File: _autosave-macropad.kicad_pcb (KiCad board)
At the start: 2 copper layers, 34 parts, among them SW1 RotaryEncoder_Switch, U1 MOUDLE-SEEEDUINO-XIAO

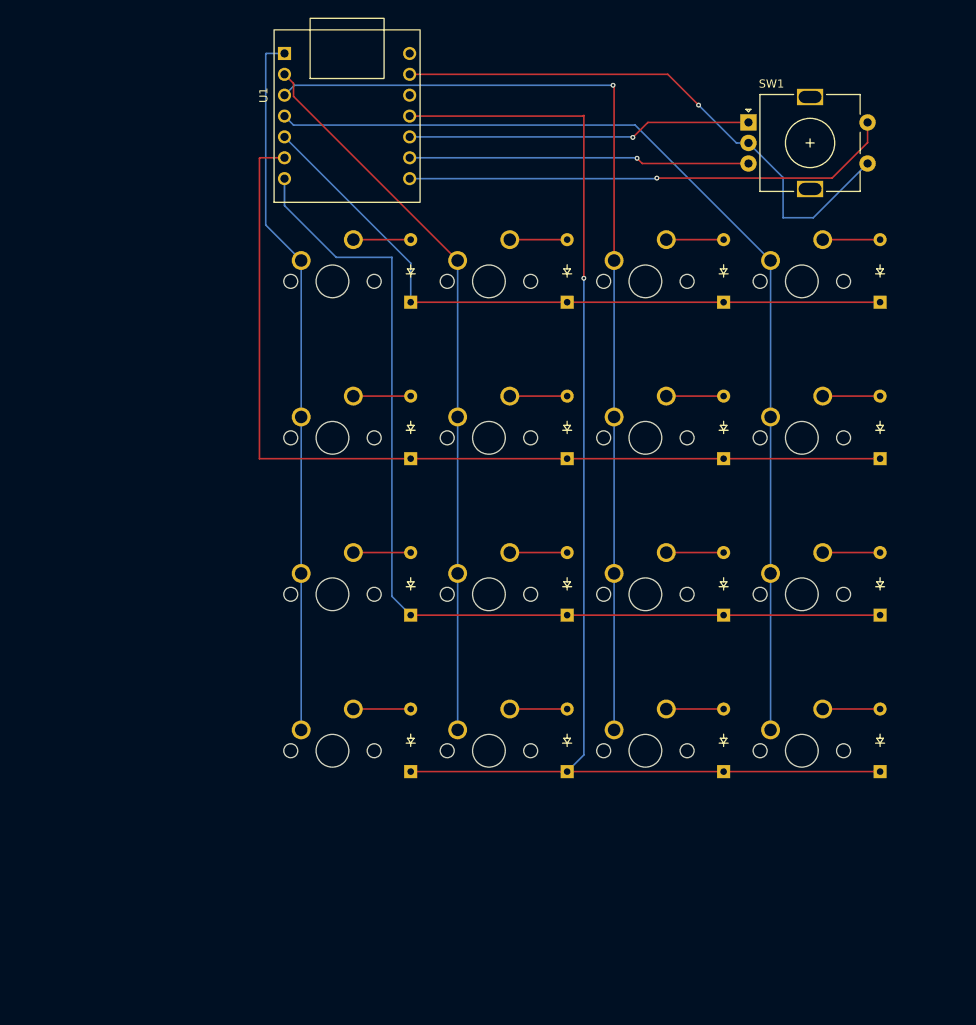
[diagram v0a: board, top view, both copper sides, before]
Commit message: Make cutout and holes
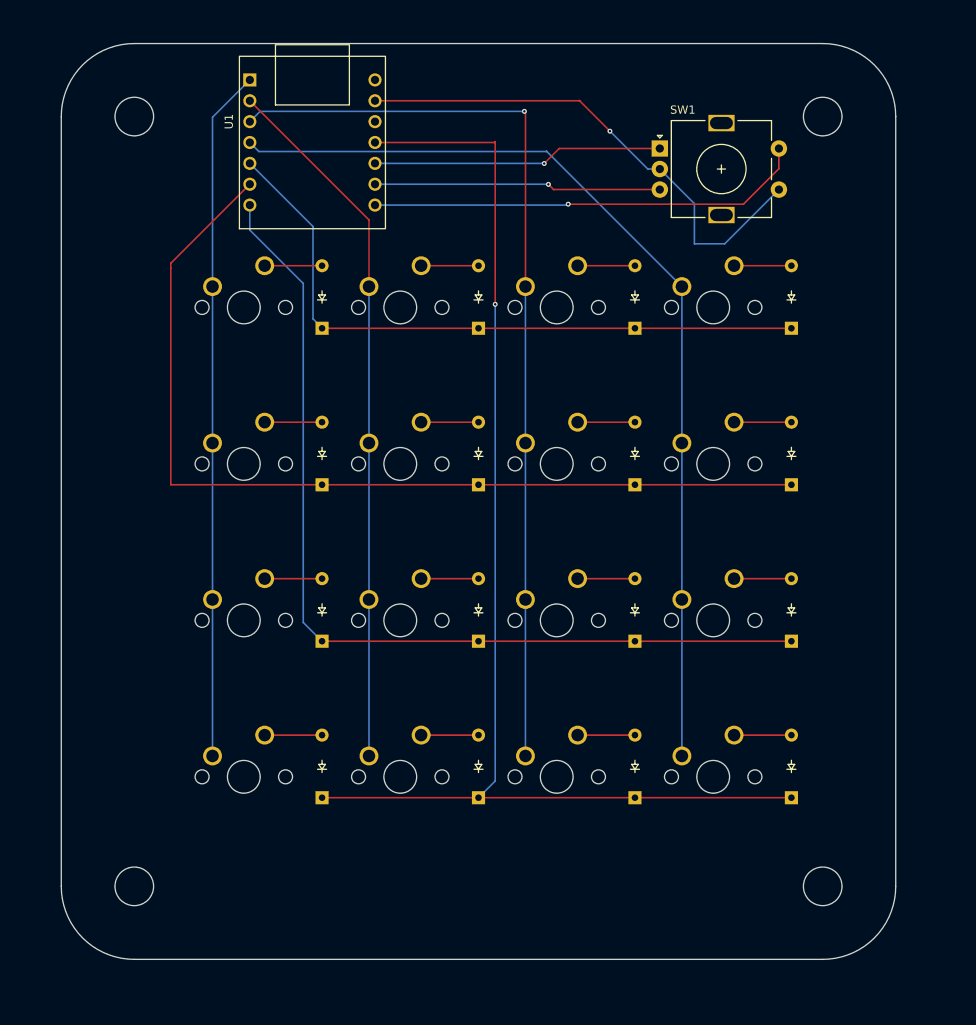
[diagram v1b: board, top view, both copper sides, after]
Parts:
- moved D22 11.3 mm to (165.1, 81.9)
- moved D18 11.3 mm to (165.1, 62.9)
- moved S1 11.3 mm to (117.5, 60.3)
- moved S3 11.3 mm to (155.6, 60.3)
- moved D26 11.3 mm to (165.1, 101.0)
- moved D30 11.3 mm to (165.1, 120.0)
- moved S11 11.3 mm to (155.6, 98.4)
- moved S13 11.3 mm to (117.5, 117.5)
- moved S15 11.3 mm to (155.6, 117.5)
- moved S5 11.3 mm to (117.5, 79.4)
- moved S7 11.3 mm to (155.6, 79.4)
- moved S9 11.3 mm to (117.5, 98.4)
- moved SW1 11.3 mm to (149.1, 41.0)
- moved D19 11.3 mm to (108.0, 81.9)
- moved D1 11.3 mm to (108.0, 62.9)
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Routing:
- net ROW2: track 120.6 -> 113.9 mm
- net ROW3: track 159.1 -> 152.6 mm
- net COL3: track 123.6 -> 117.1 mm
- net EC11SW: track 60.0 -> 53.5 mm
- net COL2: track 119.0 -> 112.5 mm
- net EC11B: track 41.5 -> 35.0 mm
- net EC11A: track 42.0 -> 35.5 mm
- net GND: track 68.6 -> 62.1 mm
- net ROW0: track 83.6 -> 80.9 mm
- net COL1: track 88.6 -> 85.8 mm
- net COL0: track 86.4 -> 84.2 mm
- net ROW1: track 115.2 -> 116.1 mm
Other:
- board outline added: 101.6 x 111.5 mm

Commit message: Add graphics and redo filled zones
Additionally edge cuts were redone to correct mistake with the MCU's position relative to the PCB
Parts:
- added G***: LOGO, graphics:flag_big, F.Cu at (82.2, 70.6)
- added G***: LOGO, graphics:username, F.Cu at (116.3, 133.7)
- added G***: LOGO, graphics:white, F.Cu at (120.3, 138.0)
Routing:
- added copper zone on B.Cu, net COL0
- added copper zone on F.Cu, net COL0
